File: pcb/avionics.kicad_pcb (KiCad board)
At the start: 2 copper layers, 89.5 x 48 mm, 115 parts, among them IC101 STM32F405VGT, IC102 ADP3335, IC201 MAX-7Q, IC701 ADXL345, IC702 L3G4200D, IC703 MS5611-01BA03, IC704 HMC5883L, M3_MOUNT VAL**, P101 CONN_01X02, P102 CONN_01X04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

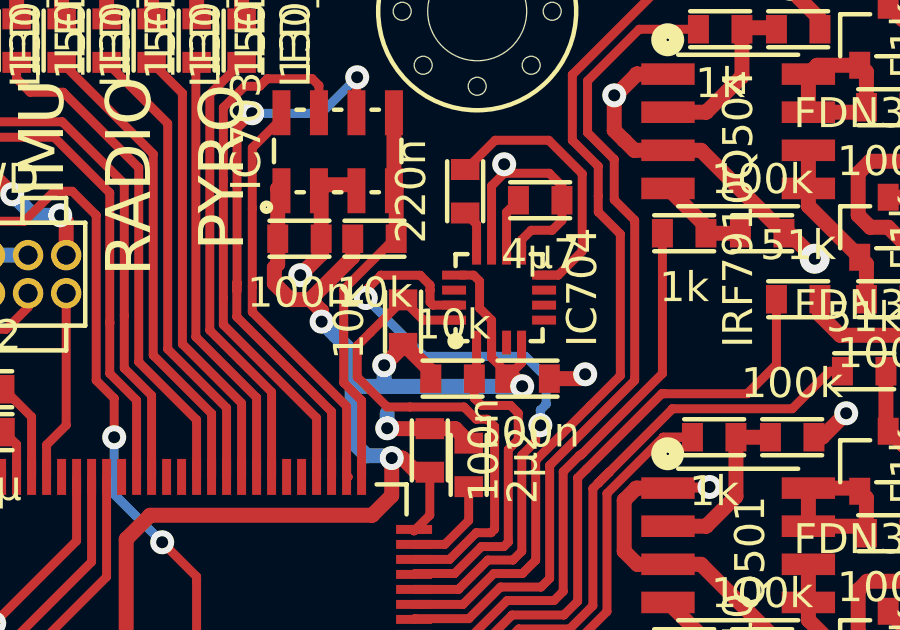
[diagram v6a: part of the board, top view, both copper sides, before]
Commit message: remove copper under magno
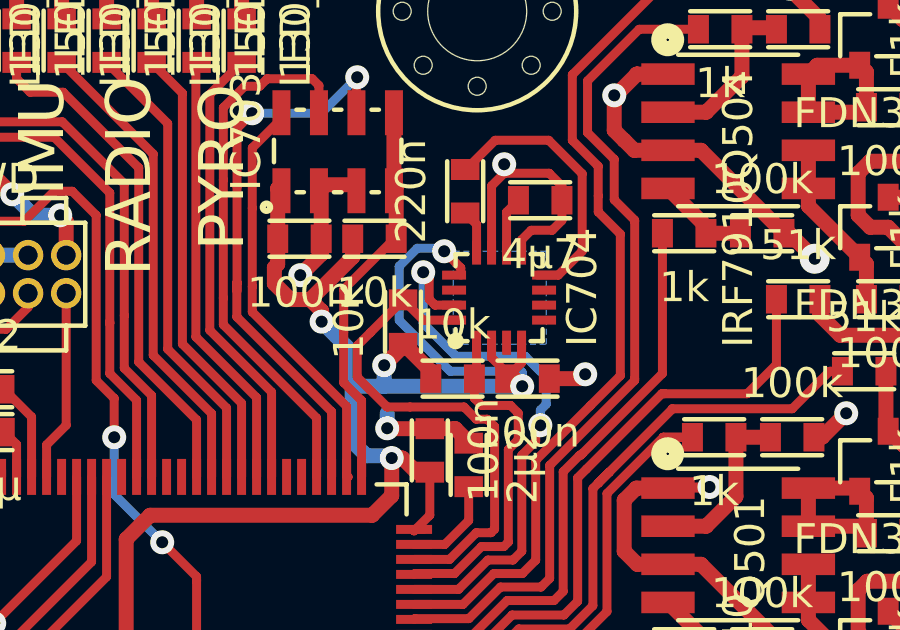
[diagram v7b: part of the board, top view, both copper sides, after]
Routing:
- net +3V3: track 355.7 -> 362.9 mm, vias 16 -> 17
- net /Inertial Measurement/MAGNO_DRDY: track 21.7 -> 18.9 mm

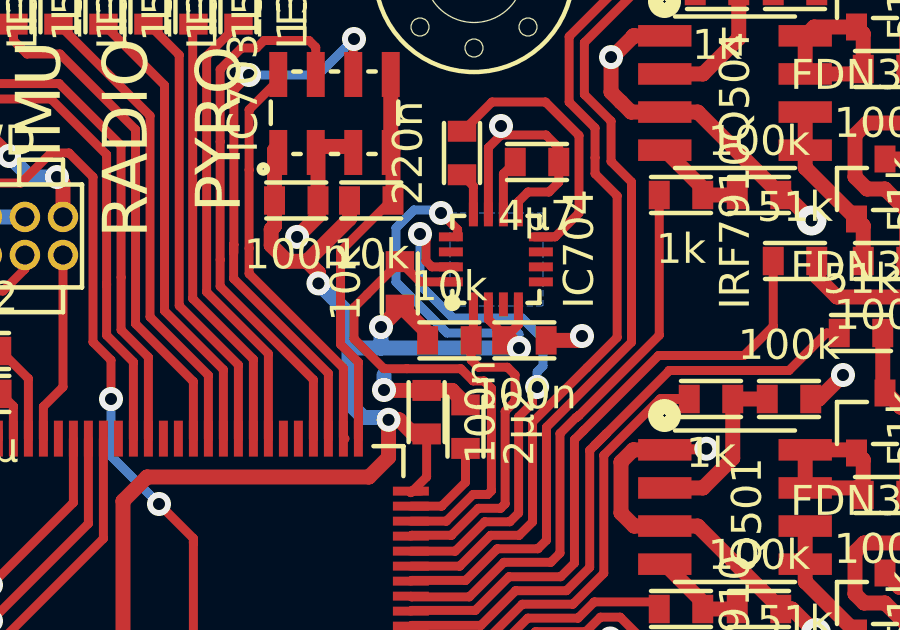
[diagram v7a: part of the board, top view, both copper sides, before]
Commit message: tidy up removed copper under magno
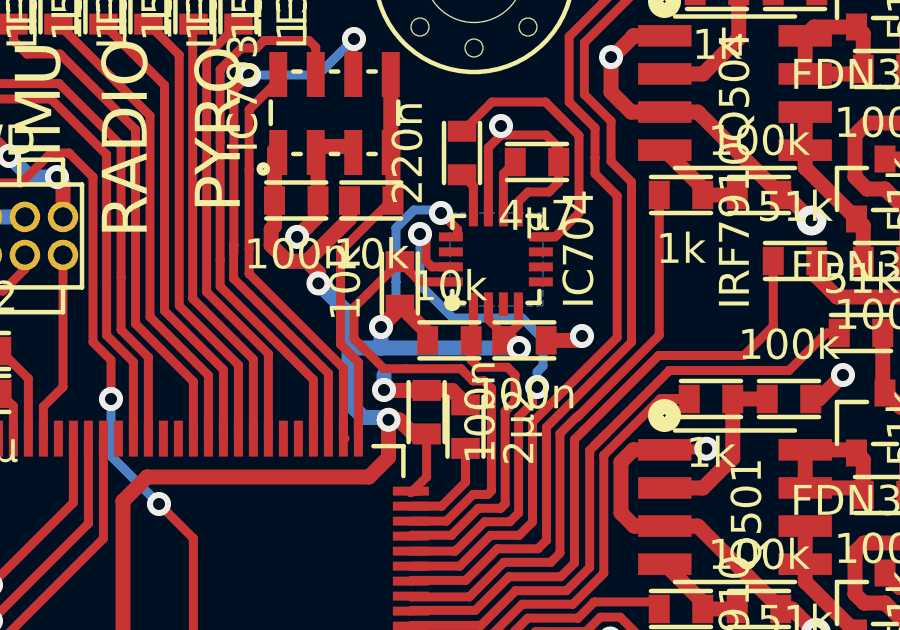
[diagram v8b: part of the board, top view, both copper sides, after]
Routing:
- net +3V3: track 362.9 -> 359.4 mm
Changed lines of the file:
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@@
     (thickness 1.6)
     (drawings 72)
-    (tracks 1430)
+    (tracks 1428)
     (zones 0)
     (modules 115)
@@
   (segment (start 161.125 79.6) (end 162.1 79.6) (width 0.3) (layer F.Cu) (net 1))
   (segment (start 162.1 79.6) (end 167.6 85.1) (width 0.3) (layer F.Cu) (net 1))
-  (segment (start 157.9544 53.796) (end 157.9544 53.5544) (width 0.3) (layer F.Cu) (net 2))
-  (segment (start 160 57.036398) (end 160 57.5) (width 0.3) (layer B.Cu) (net 2))
-  (segment (start 159.963602 57) (end 160 57.036398) (width 0.3) (layer B.Cu) (net 2))
-  (segment (start 157.6 57) (end 159.963602 57) (width 0.3) (layer B.Cu) (net 2))
-  (segment (start 155.9 55.3) (end 157.6 57) (width 0.3) (layer B.Cu) (net 2))
-  (segment (start 155.9 53.5) (end 155.9 55.3) (width 0.3) (layer B.Cu) (net 2))
-  (segment (start 156.5 52.9) (end 155.9 53.5) (width 0.3) (layer B.Cu) (net 2))
-  (segment (start 157.3 52.9) (end 156.5 52.9) (width 0.3) (layer B.Cu) (net 2))
-  (segment (start 157.4 53) (end 157.3 52.9) (width 0.3) (layer B.Cu) (net 2))
-  (via (at 157.4 53) (size 0.8) (layers F.Cu B.Cu) (net 2))
+  (segment (start 155.9 55.3) (end 155.9 56.3) (width 0.3) (layer B.Cu) (net 2))
   (segment (start 157.9544 53.5544) (end 157.4 53) (width 0.3) (layer F.Cu) (net 2))
+  (via (at 157.4 53) (size 0.8) (layers F.Cu B.Cu) (net 2))
+  (segment (start 157.4 53) (end 157.3 52.9) (width 0.3) (layer B.Cu) (net 2))
+  (segment (start 157.3 52.9) (end 156.5 52.9) (width 0.3) (layer B.Cu) (net 2))
+  (segment (start 156.5 52.9) (end 155.9 53.5) (width 0.3) (layer B.Cu) (net 2))
+  (segment (start 155.9 53.5) (end 155.9 55.3) (width 0.3) (layer B.Cu) (net 2))
+  (segment (start 157.9544 53.796) (end 157.9544 53.5544) (width 0.3) (layer F.Cu) (net 2))
+  (segment (start 155.9 56.3) (end 155.4 56.8) (width 0.3) (layer B.Cu) (net 2))
   (segment (start 141.2 77.4562) (end 141.2 75.7) (width 0.5) (layer F.Cu) (net 2))
   (segment (start 155.6512 61.1488) (end 155.6512 59.8932) (width 0.5) (layer F.Cu) (net 2))
